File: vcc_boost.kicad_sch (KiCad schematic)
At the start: 30 parts, among them J1201 RFBT, J1202 RDAC, Q1201 SQJ974EP, U1201 LM5122MHX/NOPB, U1202 DAC53401DSGR

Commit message: subcircuit layout + minor schematic updates
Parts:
- added C1215, C1216, C1217, C1218, C1219: 220uF 100V, BR_Passives:C_Elec_12.5x12.5, symbol BR_Capacitors_Electrolytic:C_Alum_220uF_100V_20%_SMD
- NT1201: footprint BR_Virtual_Parts:Net_Tie_0201_1608Metric -> BR_Virtual_Parts:NetTie-2_SMD_Pad_3.88mm_wide; symbol BR_Virtual_Parts:Net_Tie_0201 -> BR_Virtual_Parts:NetTie-2_3.88mm
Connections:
- net PGND: now also C1215.2, C1216.2, C1217.2, C1218.2, C1219.2
- net VOUT: now also C1215.1, C1216.1, C1217.1, C1218.1, C1219.1
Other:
- moved on the sheet: C1201, C1202, C1203, C1204, C1205, C1206, C1207, C1208, C1209, C1210, C1211, C1212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

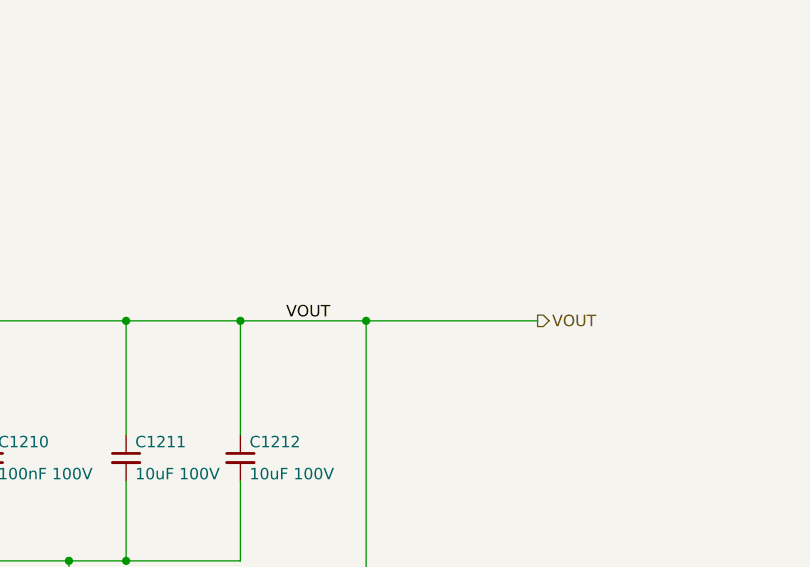
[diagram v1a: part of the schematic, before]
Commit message: adding test pads + minor schematic edits
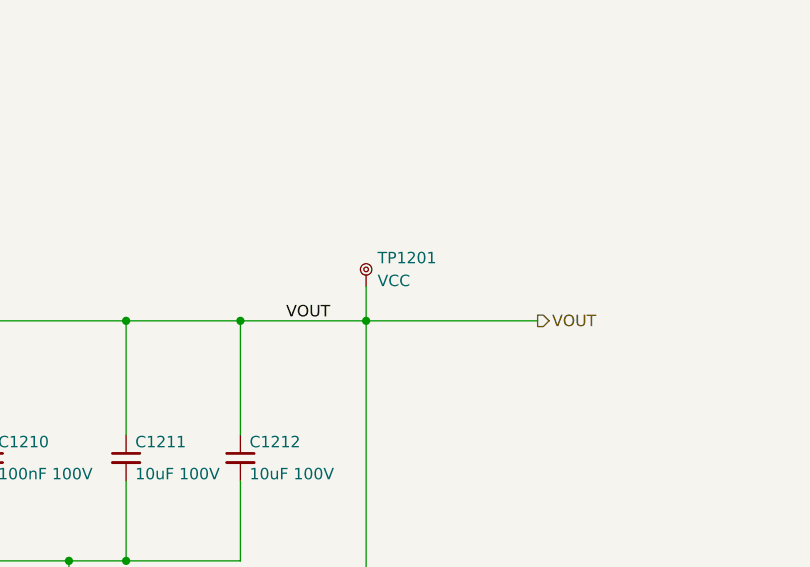
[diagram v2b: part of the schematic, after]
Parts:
- added TP1201: VCC, BR_Connectors:TEST-TH_BD2.54-P1.4_RED, symbol BR_Connectors:TP_Ring_PTH
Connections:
- net VOUT: now also TP1201.1
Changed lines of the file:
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@@
 	(wire
 		(pts
+			(xy 317.5 96.52) (xy 317.5 100.33)
+		)
+		(stroke
+			(width 0)
+			(type default)
+		)
+	)
+	(wire
+		(pts
 			(xy 64.77 118.11) (xy 54.61 118.11)
 		)
@@
 					(unit 1)
 				)
+			)
+		)
+	)
+	(symbol
+		(lib_id "BR_Connectors:TP_Ring_PTH")
+		(at 317.5 96.52 0)
+		(unit 1)
+		(exclude_from_sim no)
+		(in_bom yes)
+		(on_board yes)
+		(dnp no)
+		(fields_autoplaced yes)
+		(property "Reference" "TP1201"
+			(at 318.77 93.3449 0)
+			(effects
+				(font
+					(size 1.27 1.27)
+				)
+				(justify left)
+			)
+		)
+		(property "Value" "VCC"
+			(at 318.77 95.8849 0)
+			(effects
+				(font
+					(size 1.27 1.27)
+				)
+				(justify left)
+			)
+		)
+		(property "Footprint" "BR_Connectors:TEST-TH_BD2.54-P1.4_RED"
+			(at 317.5 20.32 0)
+			(effects
+				(font
+					(size 1.27 1.27)
+				)
+				(justify left)
+				(hide yes)
+			)
+		)
+		(property "Datasheet" "https://wmsc.lcsc.com/wmsc/upload/file/pdf/v2/lcsc/2307040929_ronghe-RH-5000_C5277086.pdf"
+			(at 317.5 22.86 0)
+			(effects
+				(font
+					(size 1.27 1.27)
+				)
+				(justify left)
+				(hide yes)
+			)
+		)
+		(property "Description" "Ring Test Point for Probe(s) PTH"
+			(at 317.5 25.4 0)
+			(effects
+				(font
+					(size 1.27 1.27)
+				)
+				(justify left)
+				(hide yes)
+			)
+		)
+		(property "Manufacturer" "ronghe"
+			(at 317.5 27.94 0)
+			(effects
+				(font
+					(size 1.27 1.27)
+				)
+				(justify left)
+				(hide yes)
+			)
+		)
+		(property "Manufacturer Part Num" "RH-5000"
+			(at 317.5 30.48 0)
+			(effects
+				(font
+					(size 1.27 1.27)
+				)
+				(justify left)
+				(hide yes)
+			)
+		)
+		(property "BRE Number" "BRE-000074"
+			(at 317.5 33.02 0)
+			(effects
+				(font
+					(size 1.27 1.27)
+				)
+				(justify left)
+				(hide yes)
+			)
+		)
+		(property "Supplier 1" "DigiKey"
+			(at 317.5 35.56 0)
+			(effects
+				(font
+					(size 1.27 1.27)
+				)
+				(justify left)
+				(hide yes)
+			)
+		)
+		(property "Supplier Part Num 1" "~"
+			(at 317.5 38.1 0)
+			(effects
+				(font
+					(size 1.27 1.27)
+				)
+				(justify left)
+				(hide yes)
+			)
+		)
+		(property "Supplier 2" "Mouser"
+			(at 317.5 40.64 0)
+			(effects
+				(font
+					(size 1.27 1.27)
+				)
+				(justify left)
+				(hide yes)
+			)
+		)
+		(property "Supplier Part Num 2" "~"
+			(at 317.5 43.18 0)
+			(effects
+				(font
+					(size 1.27 1.27)
+				)
+				(justify left)
+				(hide yes)
+			)
+		)
+		(property "Supplier 3" "JLCPCB"
+			(at 317.5 45.72 0)
+			(effects
+				(font
+					(size 1.27 1.27)
+				)
+				(justify left)
+				(hide yes)
+			)
+		)
+		(property "Supplier Part Num 3" "C5277086"
+			(at 317.5 48.26 0)
+			(effects
+				(font
+					(size 1.27 1.27)
+				)
+				(justify left)
+				(hide yes)
+			)
+		)
+		(property "Label" "LABEL"
+			(at 317.5 50.8 0)
+			(effects
+				(font
+					(size 1.27 1.27)
+				)
+				(justify left)
+				(hide yes)
+			)
+		)
+		(property "JLCPCB Part Num" "C5277086"
+			(at 317.5 53.34 0)
+			(effects
+				(font
+					(size 1.27 1.27)
+				)
+				(justify left)
+				(hide yes)
+			)
+		)
+		(pin "1"
+		)
+		(instances
+			(project ""
+				(path "/2a5ce3ef-537a-4122-a1be-ef76186bc0d7/774f2c6c-c15c-4713-acf0-4edb2ec6be20/f57da81d-26f9-4e44-8192-6054ea342dd6"
+					(reference "TP1201")
+					(unit 1)
+				)

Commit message: various improvements
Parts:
- TP1201: value VCC -> VTX
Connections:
- net VOUT renamed VTX
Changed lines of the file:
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@@
 		)
 	)
-	(label "VOUT"
+	(label "VTX"
 		(at 308.61 100.33 0)
 		(effects
@@
 		)
 	)
-	(hierarchical_label "VOUT"
+	(hierarchical_label "VTX"
 		(shape output)
 		(at 336.55 100.33 0)
@@
 			)
 		)
-		(property "Value" "VCC"
+		(property "Value" "VTX"
 			(at 318.77 95.8849 0)
 			(effects

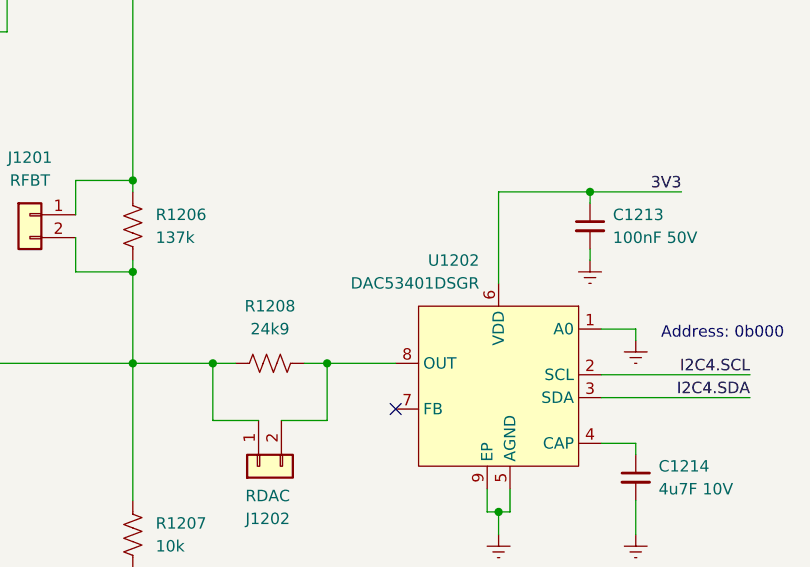
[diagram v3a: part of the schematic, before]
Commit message: clarified silkscreen labels
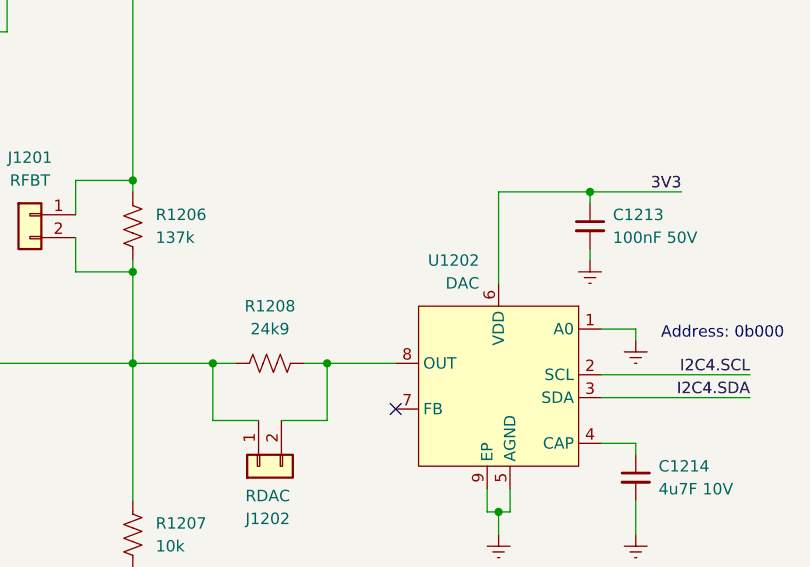
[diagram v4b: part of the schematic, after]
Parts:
- U1202: value DAC53401DSGR -> DAC
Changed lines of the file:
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@@
 			)
 		)
-		(property "Value" "DAC53401DSGR"
+		(property "Value" "DAC"
 			(at 355.9967 154.94 0)
 			(effects

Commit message: last checks + board characteristics tables
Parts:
- added TP1202: GND, BR_Connectors:TEST-TH_BD2.54-P1.4_RED, symbol BR_Connectors:TP_Ring_PTH
- C1201: JLCPCB Part Num (none) -> C60133
- C1202: JLCPCB Part Num (none) -> C576517
- C1203: JLCPCB Part Num (none) -> C471404
- C1204: JLCPCB Part Num (none) -> C76939
- C1205: JLCPCB Part Num (none) -> C77023
- C1207: JLCPCB Part Num (none) -> C962136
- C1214: JLCPCB Part Num C20044523 -> C20044522
- D1201: JLCPCB Part Num (none) -> C152543
- Q1201: JLCPCB Part Num (none) -> C727845
- R1201: JLCPCB Part Num (none) -> C138165
- R1203: JLCPCB Part Num (none) -> C114762
- U1201: JLCPCB Part Num (none) -> C77241
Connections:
- net GND: now also TP1202.1

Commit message: refactoring tx a bit
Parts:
- removed C1208, C1215, C1216, C1217, C1218, C1219: 220uF 100V, BR_Passives:C_Elec_12.5x12.5, symbol BR_Capacitors_Electrolytic:C_Alum_220uF_100V_20%_SMD
- added NT1: Net_Tie_0603, BR_Virtual_Parts:Net_Tie_0603_1608Metric, symbol BR_Virtual_Parts:Net_Tie_0603
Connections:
- net VTX: now also NT1.2; no longer C1209.2, C1210.1, C1211.1, C1212.1, J1201.1 (Pin_1), Q1201.6 (D), R1206.1, TP1201.1
- new net VTX_LOCAL: C1209.2, C1210.1, C1211.1, C1212.1, J1201.1 (Pin_1), NT1.1, Q1201.6 (D), R1206.1, TP1201.1

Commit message: Various changes to TX connectity
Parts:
- removed J1201: RFBT, BR_Connectors:PinHeader_1x02_P2.54mm_Vertical, symbol BR_Connectors_Header:Header_Socket_SIP_01x02_2.54mm_Vert_PTH
- removed J1202: RDAC, BR_Connectors:PinHeader_1x02_P2.54mm_Vertical, symbol BR_Connectors_Header:Header_Socket_SIP_01x02_2.54mm_Vert_PTH
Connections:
- net VTX: now also TP1201.1
- net VTX_LOCAL: no longer TP1201.1
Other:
- moved on the sheet: TP1201
